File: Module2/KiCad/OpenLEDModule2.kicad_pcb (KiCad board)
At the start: 2 copper layers, 29.2 x 53.1 mm, 11 parts, among them P1 CONN_01X02, P2 CONN_01X02

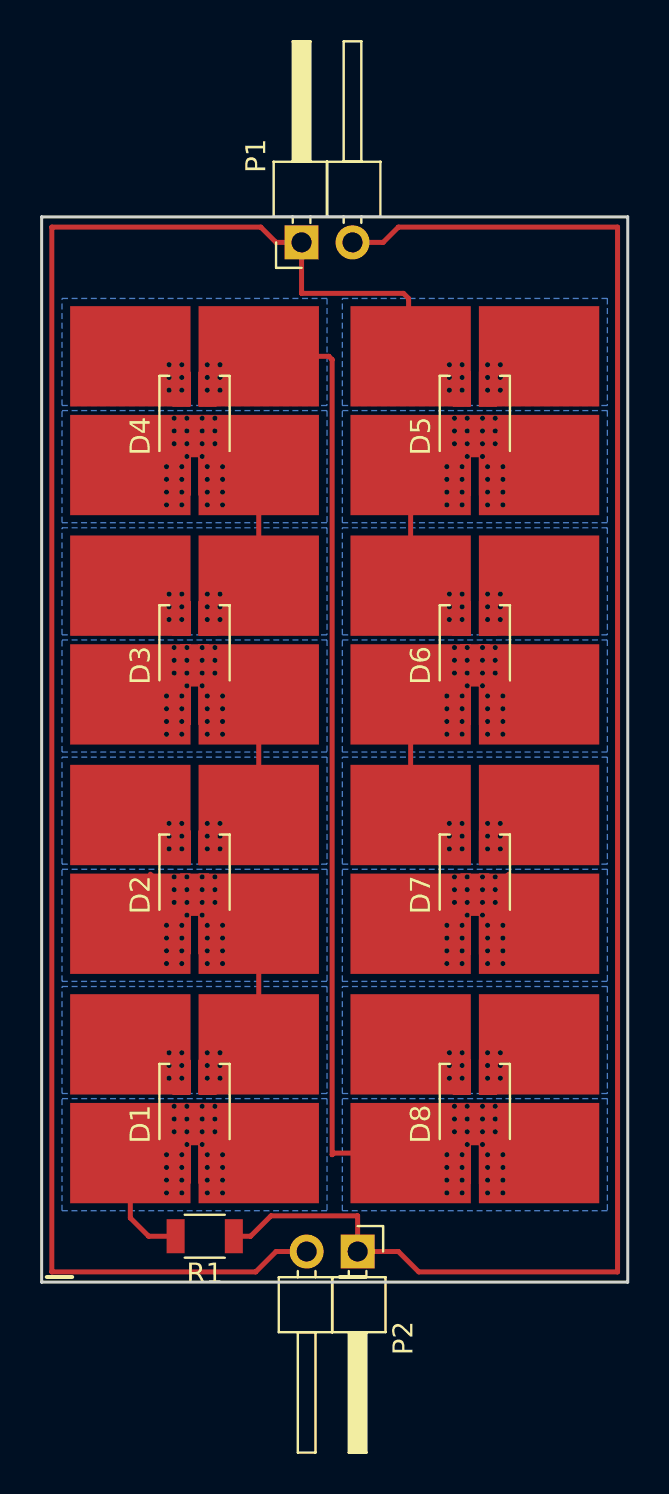
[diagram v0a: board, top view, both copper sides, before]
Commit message: Added GND filling on Module 1/2. Added Gerbers.
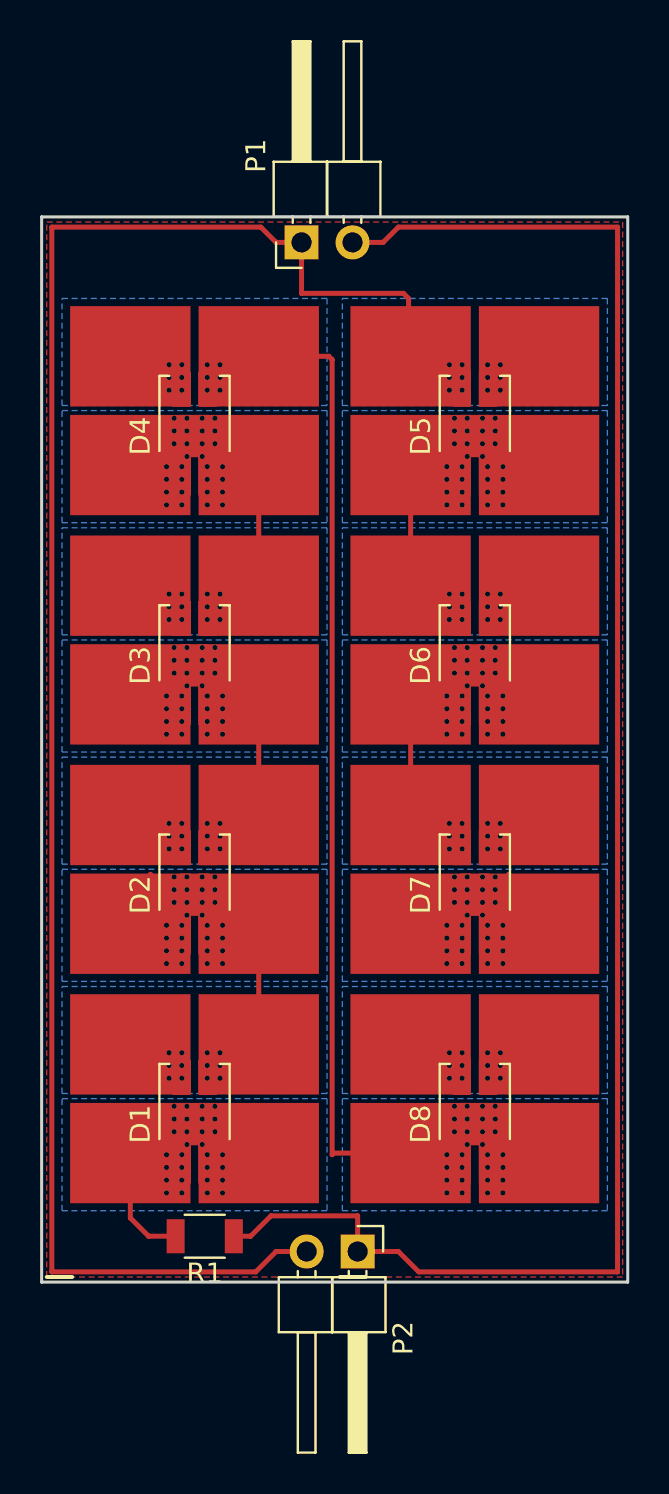
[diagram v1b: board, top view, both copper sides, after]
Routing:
- added copper zone on F.Cu, net GND
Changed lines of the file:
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@@
   (general
     (links 68)
-    (no_connects 23)
-    (area 129.718999 73.152 165.354001 153.477001)
+    (no_connects 22)
+    (area 129.718999 82.234999 159.079001 153.477001)
     (thickness 1.6)
     (drawings 9)
@@
       (linewidth 0.100000)
       (plotframeref false)
-      (viasonmask false)
+      (viasonmask true)
       (mode 1)
       (useauxorigin false)
@@
       (outputformat 1)
       (mirror false)
-      (drillshape 1)
+      (drillshape 0)
       (scaleselection 1)
       (outputdirectory ""))
@@
       )
     )
+  )
+  (zone (net 1) (net_name GND) (layer F.Cu) (hatch edge 0.508)
+    (connect_pads (clearance 0.508))
+    (min_thickness 0.254)
+    (fill yes (arc_segments 16) (thermal_gap 0.508) (thermal_bridge_width 0.508))
+    (polygon
+      (pts
+        (xy 158.75 144.272) (xy 130.048 144.272) (xy 130.048 91.694) (xy 158.75 91.694)
+      )
+    )
